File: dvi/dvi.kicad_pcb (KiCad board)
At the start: 4 copper layers, 30 x 30 mm, 61 parts, among them IC1 TLV61222DC, J1 MISC, P1 GPDI, U1 PCA9306

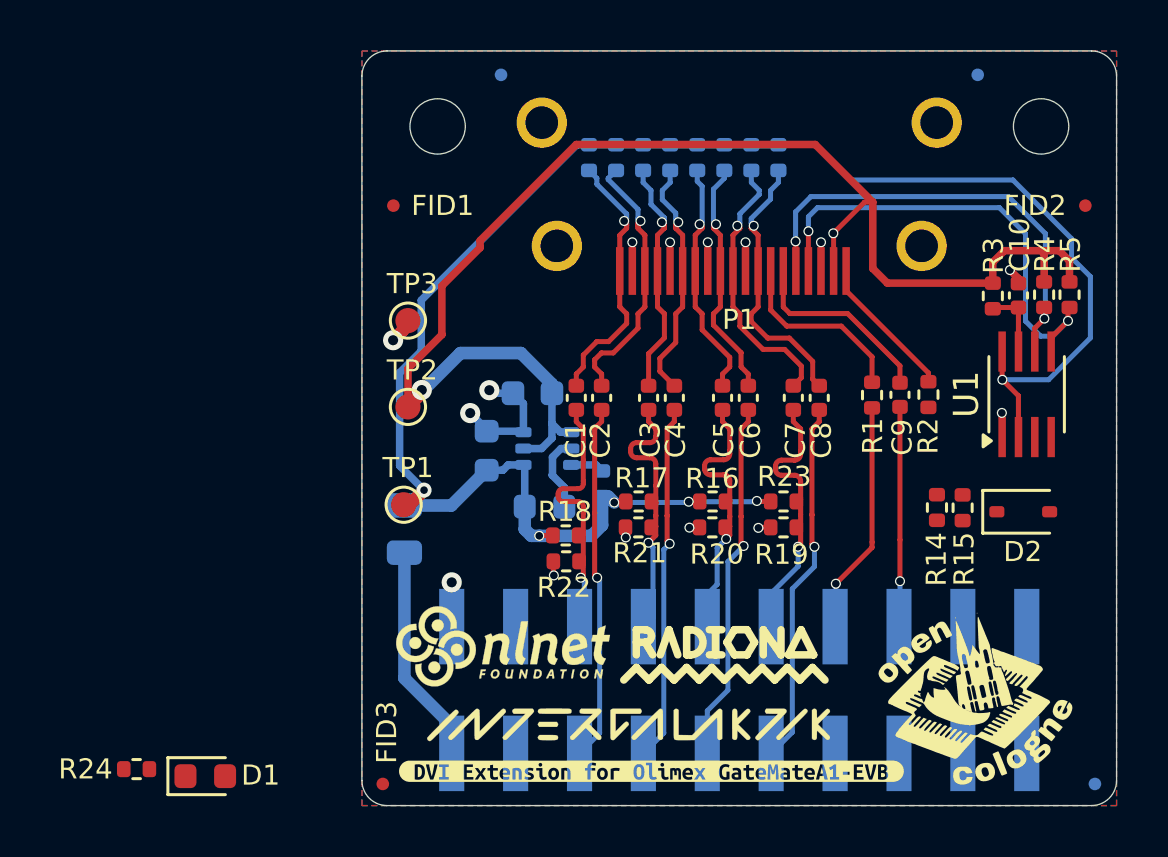
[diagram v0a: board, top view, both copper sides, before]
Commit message: Routing DVI
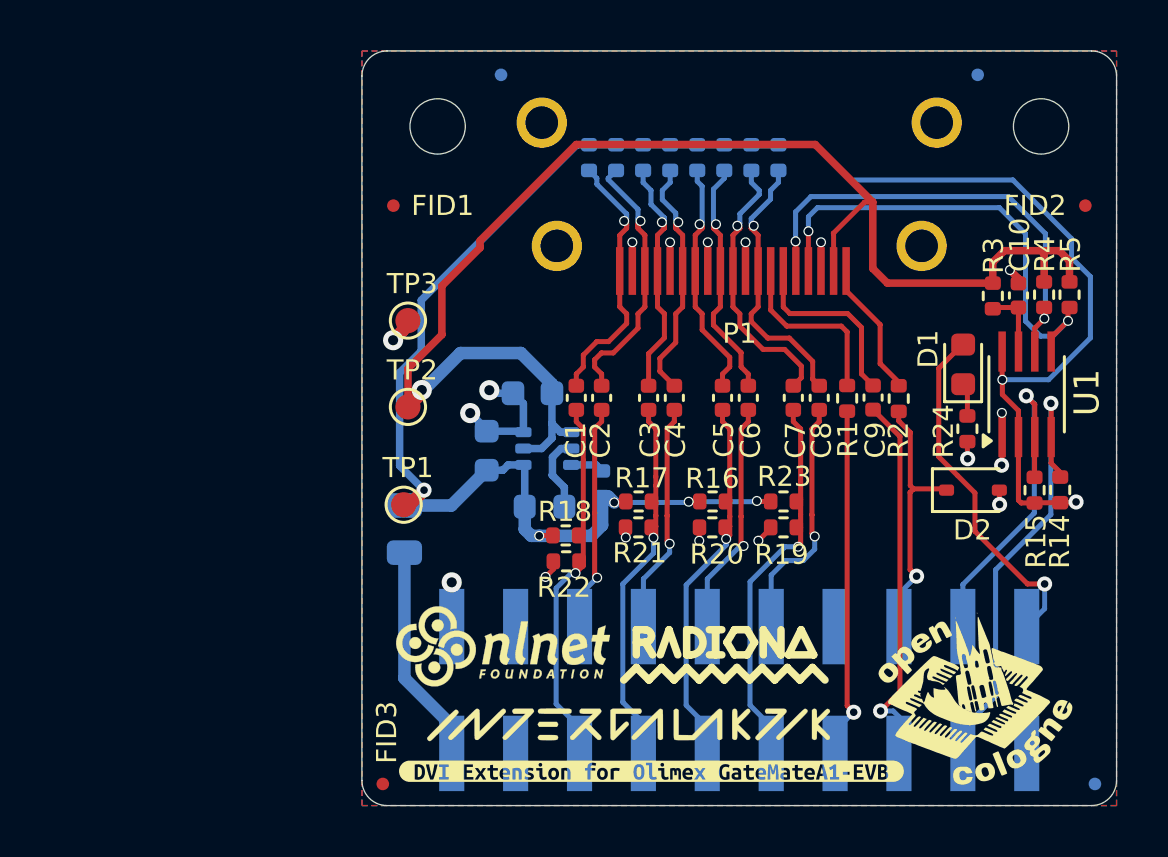
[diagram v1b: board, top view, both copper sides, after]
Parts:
- moved R24 35.7 mm to (109.3, 66.9), turned to 90 degrees
- moved D1 34.3 mm to (109.2, 64.3), turned to 90 degrees
- moved R14 4.95 mm to (113.0, 69.3)
- moved R15 2.94 mm to (112.0, 69.3)
- moved D2 2.18 mm to (109.5, 69.3)
- moved R2 1.19 mm to (106.6, 65.7)
- moved C9 1.08 mm to (105.6, 65.6)
- moved R1 1.00 mm to (104.5, 65.6)
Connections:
- J1 pad 10: GPDI_D0+ -> GPDI_D0-
- J1 pad 11: GPDI_CLK- -> GPDI_CLK+
- J1 pad 12: GPDI_CLK+ -> GPDI_CLK-
- J1 pad 13: 5V_ENABLE -> GPDI_CEC
- J1 pad 14: GPDI_CEC -> /Main Sheet/NB_B5
- J1 pad 15: GPDI_ETH- -> GPDI_ETH+
- J1 pad 16: GPDI_ETH+ -> GPDI_ETH-
- J1 pad 17: PMOD_SCL -> PMOD_SDA
- J1 pad 18: PMOD_SDA -> PMOD_SCL
- J1 pad 20: /Main Sheet/NB_B8 -> 5V_ENABLE
- J1 pad 5: GPDI_D2- -> GPDI_D2+
- J1 pad 6: GPDI_D2+ -> GPDI_D2-
- J1 pad 7: GPDI_D1- -> GPDI_D1+
- J1 pad 8: GPDI_D1+ -> GPDI_D1-
- J1 pad 9: GPDI_D0- -> GPDI_D0+
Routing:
- net PMOD_SDA: track 0.00 -> 18.4 mm, vias 0 -> 1
- net 5V_ENABLE: track 0.00 -> 14.1 mm, vias 0 -> 1
- net PMOD_SCL: track 0.00 -> 13.9 mm, vias 0 -> 1
- net GPDI_ETH-: track 0.00 -> 10.6 mm, vias 0 -> 1
- net GPDI_ETH+: track 8.75 -> 15.0 mm
- net GPDI_D2-: track 14.2 -> 9.06 mm
- net GPDI_D1-: track 14.2 -> 9.21 mm
- net /Main Sheet/+2V5: track 73.2 -> 78.2 mm, vias 6 -> 7
- net GPDI_D0-: track 14.4 -> 9.45 mm
- net GPDI_CEC: track 9.30 -> 14.0 mm
- net GPDI_CLK-: track 14.5 -> 9.91 mm
- net GPDI_CLK+: track 11.1 -> 15.6 mm
- net GPDI_D0+: track 11.0 -> 15.2 mm
- net GPDI_D2+: track 11.0 -> 15.1 mm
- net GPDI_D1+: track 11.0 -> 15.1 mm
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
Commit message: DVI update
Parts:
- removed D2: BZT52C3V6S-7-F, Diode_SMD:D_SOD-323
- added Q1: BSS138, Package_TO_SOT_SMD:SOT-23, F.Cu at (109.4, 72.2)
- added R28: 10K, Resistor_SMD:R_0402_1005Metric, F.Cu at (112.2, 73.1)
- added R29: 10K, Resistor_SMD:R_0402_1005Metric, F.Cu at (108.9, 68.5)
- moved D1 18.8 mm to (91.0, 69.2)
- moved R24 18.8 mm to (91.2, 71.8)
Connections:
- IC1 pad 6: Net-(IC1-EN) -> 5V_ENABLE
- J1 pad 16: GPDI_ETH- -> GPDI_ETH_lowV-
- J1 pad 20: 5V_ENABLE -> /Main Sheet/NB_B8
- J1 pad 4: /Main Sheet/NB_B0 -> 5V_ENABLE
- R25 pad 2: Net-(IC1-EN) -> 5V_ENABLE
- U1 pad 8: /Main Sheet/+2V5 -> /Main Sheet/VREF2
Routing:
- net +5V: track 55.1 -> 68.6 mm, vias 1 -> 3
- net GPDI_ETH_lowV-: track 0.00 -> 7.04 mm, vias 0 -> 1
- net /Main Sheet/+2V5: track 78.2 -> 81.2 mm, vias 7 -> 6
- net 5V_ENABLE: track 14.1 -> 11.7 mm, vias 1 -> 2
- net /Main Sheet/VREF2: track 2.79 -> 4.64 mm
- net Net-(IC1-EN): track 1.33 -> 0.00 mm
- net GND: track 20.0 -> 19.1 mm, vias 18 -> 53
- net GPDI_ETH-: track 10.6 -> 11.4 mm, vias 1 -> 0
